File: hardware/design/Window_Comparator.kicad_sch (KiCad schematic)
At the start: 5 parts, among them U1101 LM393

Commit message: Editorial change
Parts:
- R1103: renamed from R1102; value 50k -> 51k
- renumbered R1103 to R1102

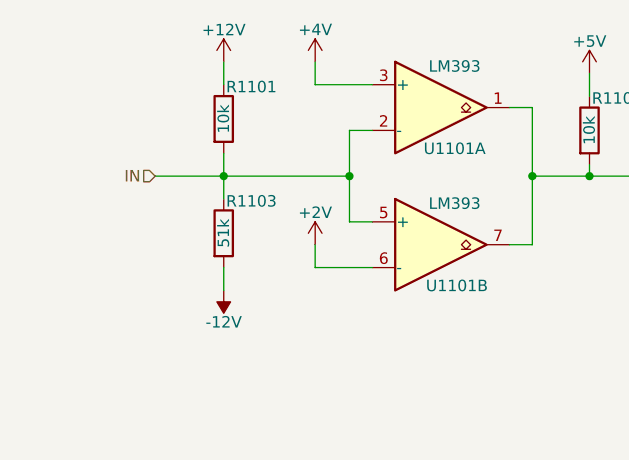
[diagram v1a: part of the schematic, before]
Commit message: Quality assessment - Changes
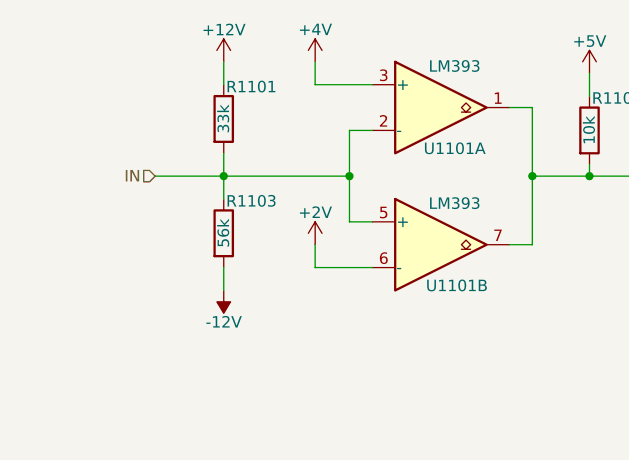
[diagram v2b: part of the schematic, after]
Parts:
- R1101: value 10k -> 33k
- R1103: value 51k -> 56k
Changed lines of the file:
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@@
 			)
 		)
-		(property "Value" "10k"
+		(property "Value" "33k"
 			(at 52.07 46.99 90)
 			(effects
@@
 			)
 		)
-		(property "Value" "51k"
+		(property "Value" "56k"
 			(at 52.07 59.69 90)
 			(effects

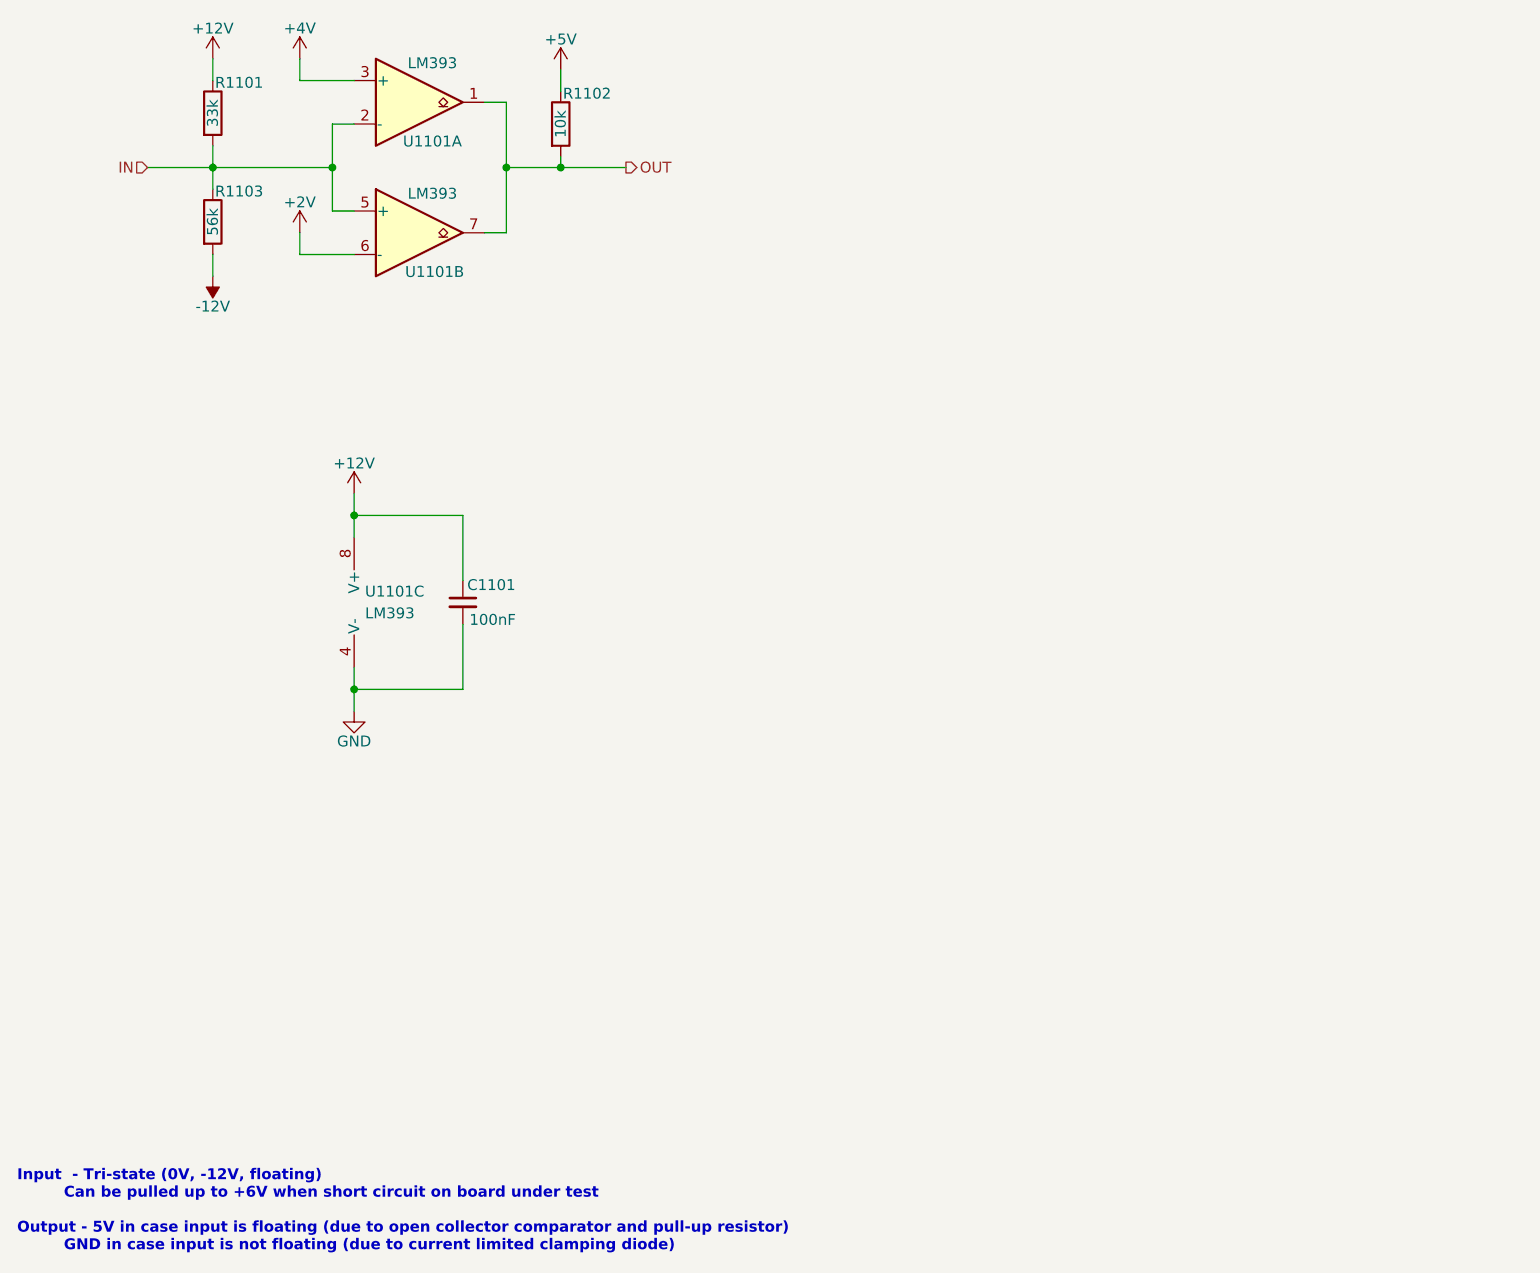
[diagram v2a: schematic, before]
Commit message: Simulating alternative power supply
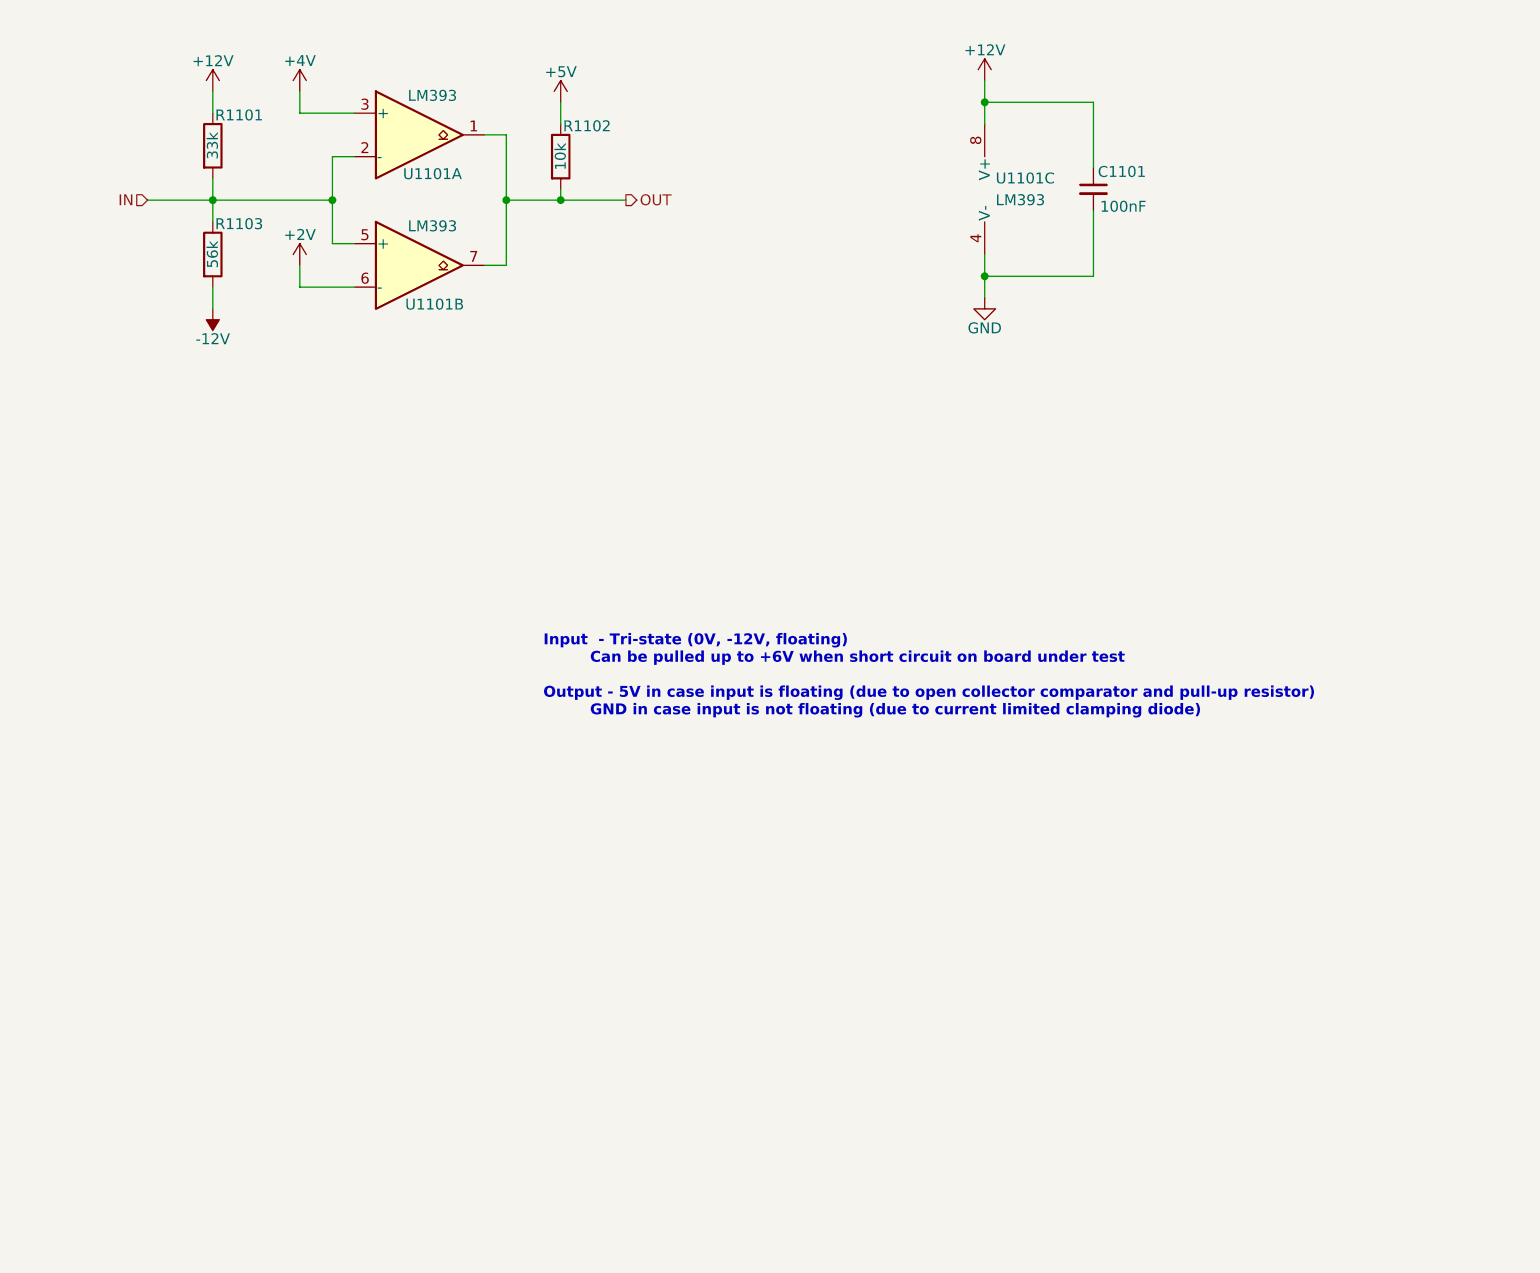
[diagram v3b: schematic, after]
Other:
- moved on the sheet: C1101, R1101, R1102, R1103, U1101A, U1101B, U1101C

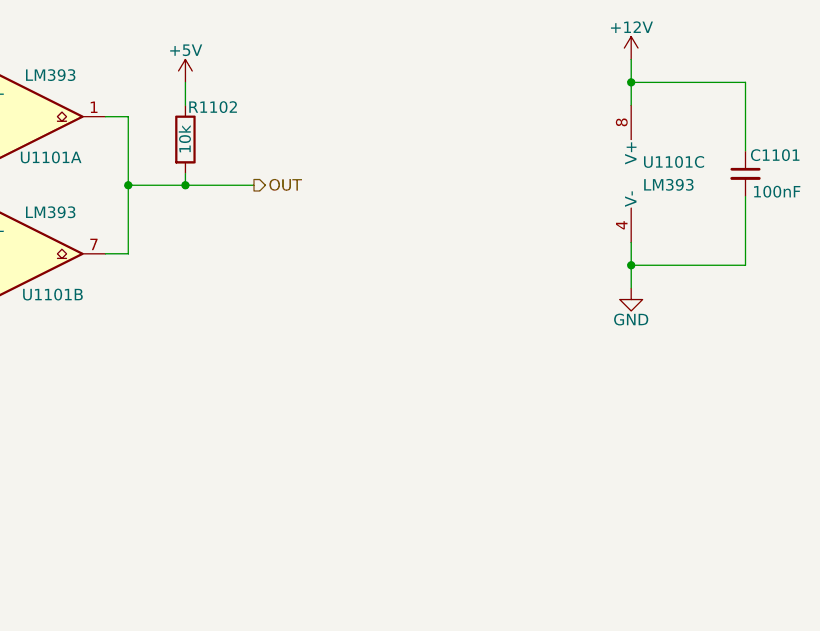
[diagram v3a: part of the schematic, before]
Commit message: Added proof of concept Window comparator
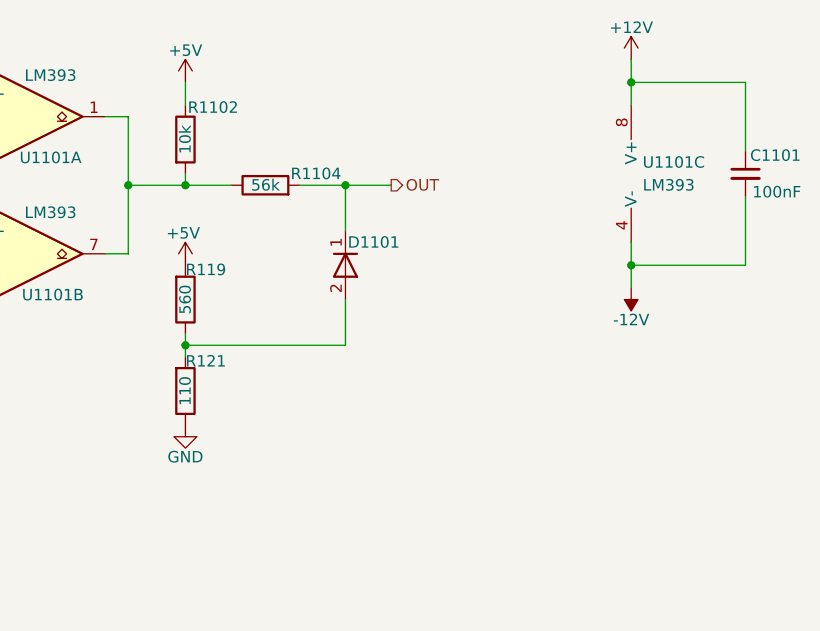
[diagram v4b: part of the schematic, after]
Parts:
- added D1101: D, Diode_THT:D_5W_P10.16mm_Horizontal, symbol Simulation_SPICE:D
- added R1104: 56k, Resistor_THT:R_Axial_DIN0207_L6.3mm_D2.5mm_P7.62mm_Horizontal, symbol Device:R
- added R119: 560, Resistor_THT:R_Axial_DIN0207_L6.3mm_D2.5mm_P7.62mm_Horizontal, symbol Device:R
- added R121: 110, Resistor_THT:R_Axial_DIN0207_L6.3mm_D2.5mm_P7.62mm_Horizontal, symbol Device:R
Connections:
- net +5V: now also R119.2
- net -12V: now also C1101.2, U1101.4 (V-)
- net GND: now also R121.1; no longer C1101.2, U1101.4 (V-)
- net OUT: now also D1101.1 (K), R1104.2; no longer R1102.2, U1101.1, U1101.7
- new net: R1102.2, R1104.1, U1101.1, U1101.7
- new net: D1101.2 (A), R119.1, R121.2

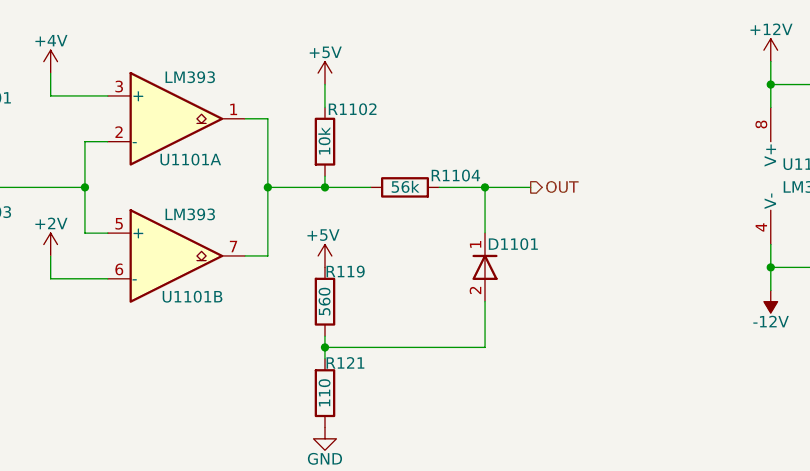
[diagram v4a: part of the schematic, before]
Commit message: Finished proof of concept Window_Comparator and integration test Window_Comparator with Cascaded_74xx165
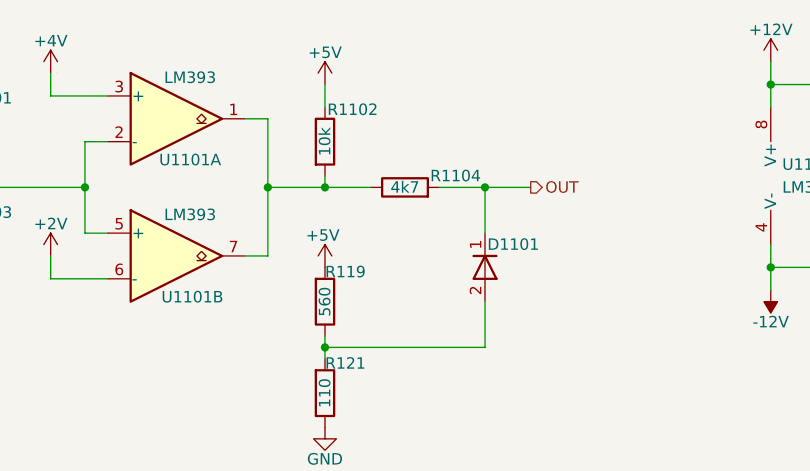
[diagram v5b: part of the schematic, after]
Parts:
- R1104: value 56k -> 4k7
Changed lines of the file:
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@@
 			)
 		)
-		(property "Value" "56k"
+		(property "Value" "4k7"
 			(at 101.6 57.15 90)
 			(effects

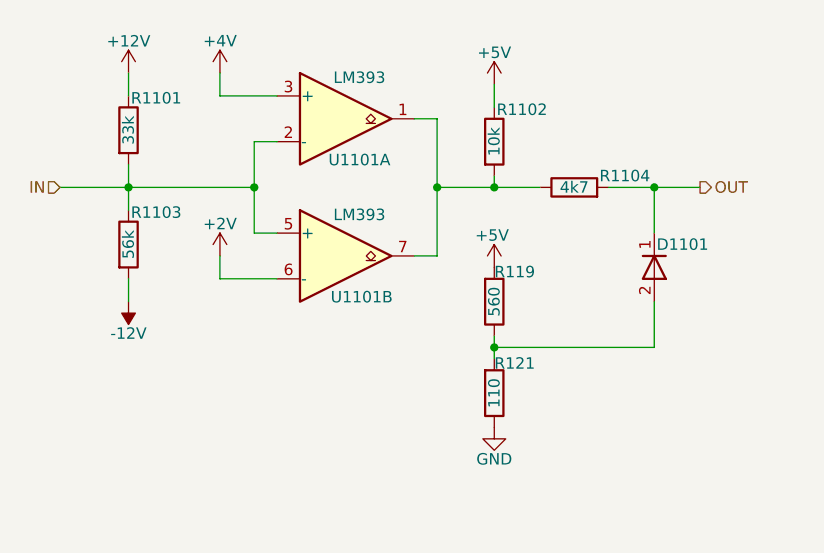
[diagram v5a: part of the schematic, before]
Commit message: Finished proof of concept Relay_Driver
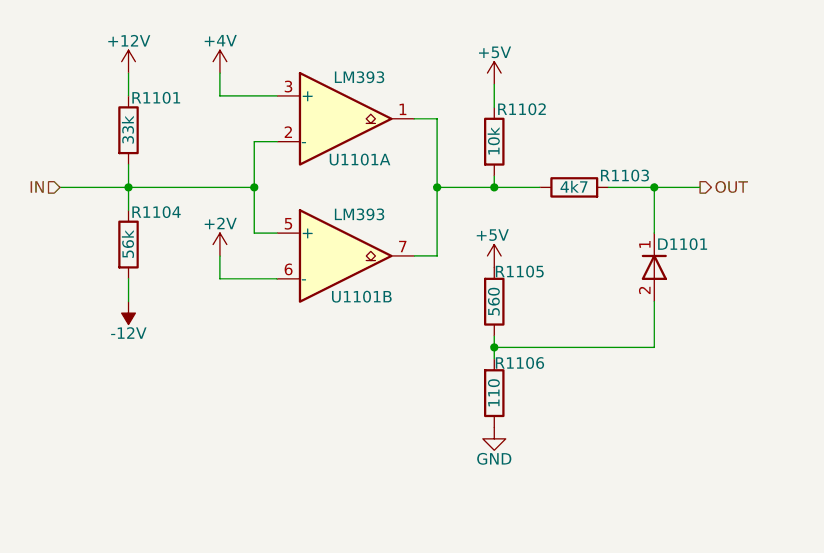
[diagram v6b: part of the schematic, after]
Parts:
- removed R119: 560, Resistor_THT:R_Axial_DIN0207_L6.3mm_D2.5mm_P7.62mm_Horizontal, symbol Device:R
- removed R121: 110, Resistor_THT:R_Axial_DIN0207_L6.3mm_D2.5mm_P7.62mm_Horizontal, symbol Device:R
- added R1105: 560, Resistor_THT:R_Axial_DIN0207_L6.3mm_D2.5mm_P7.62mm_Horizontal, symbol Device:R
- added R1106: 110, Resistor_THT:R_Axial_DIN0207_L6.3mm_D2.5mm_P7.62mm_Horizontal, symbol Device:R
- renumbered R1104 to R1103, R1103 to R1104
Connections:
- net +5V: now also R1105.2
- net GND: now also R1106.1
- net at D1101.2 (A): now also R1105.1, R1106.2

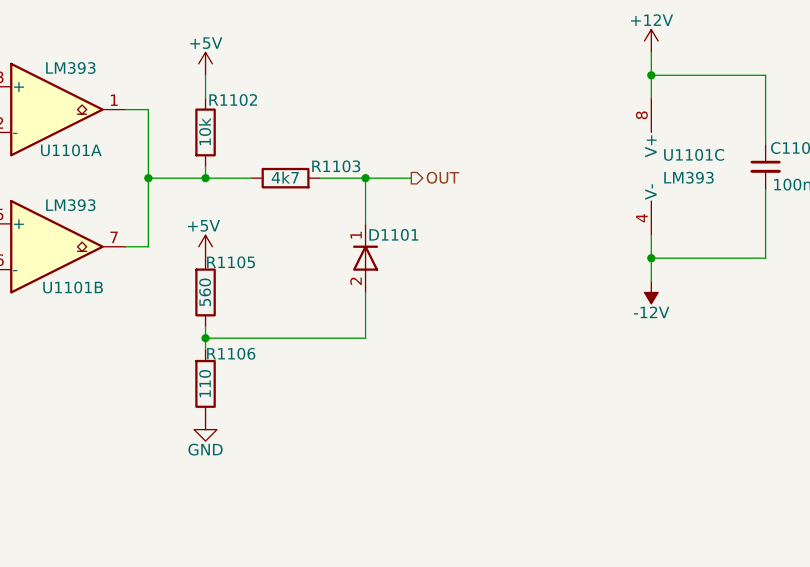
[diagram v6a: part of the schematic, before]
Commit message: Added Setter_Getter proof of concept and Setter_Getter 74xx165 and 74xx595 integration proof of concept
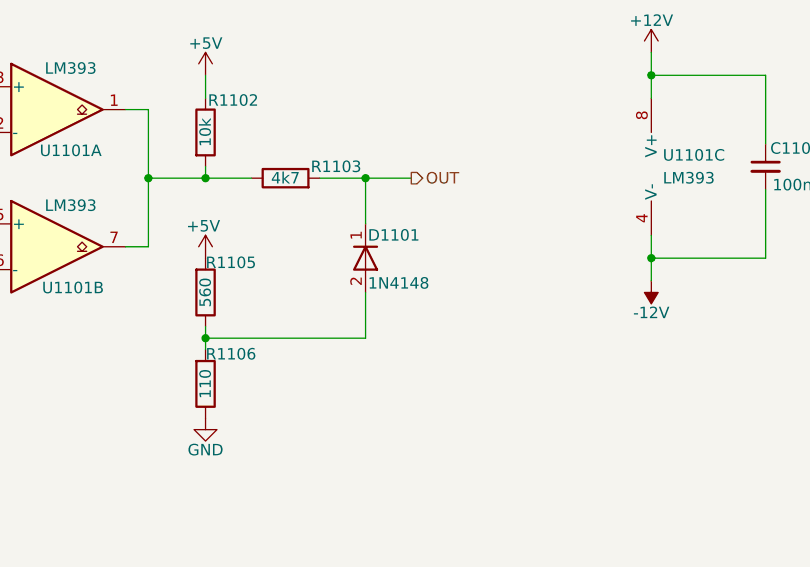
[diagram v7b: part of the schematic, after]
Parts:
- D1101: value D -> 1N4148
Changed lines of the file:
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@@
 			)
 		)
-		(property "Value" "D"
-			(at 113.03 67.3099 90)
+		(property "Value" "1N4148"
+			(at 110.744 68.834 90)
 			(effects
 				(font
@@
 				)
 				(justify left)
-				(hide yes)
 			)
 		)

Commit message: File cleanup
Added final schematics
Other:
- note added: "Input - Tri-state (0V, -12V, floating) Can be pulled up to +6V when there is short circuit on the board under test Output - 5V in case input is floating (due to open collector comparator and pull-up resistor) GND in case input is not floating (due to current limited clamping diode)"
- note removed: "Input - Tri-state (0V, -12V, floating) Can be pulled up to +6V when short circuit on board under test Output - 5V in case input is floating (due to open collector comparator and pull-up resistor) GND in case input is not floating (due to current limited clamping diode)"
- moved on the sheet: R1102
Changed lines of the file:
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@@
 	(title_block
 		(title "VersaLogic board tester")
-		(date "2025-08-13")
-		(rev "1.0.alpha")
+		(date "2025-09-09")
+		(rev "1.0")
 		(comment 1 "Copyright (c) 2025 by Filip Pynckels & Robin Pynckels")
 	)
-	(text "Input  - Tri-state (0V, -12V, floating)\n         Can be pulled up to +6V when short circuit on board under test\n\nOutput - 5V in case input is floating (due to open collector comparator and pull-up resistor)\n         GND in case input is not floating (due to current limited clamping diode)"
+	(text "Input  - Tri-state (0V, -12V, floating)\n         Can be pulled up to +6V when there is short circuit on the board under test\n\nOutput - 5V in case input is floating (due to open collector comparator and pull-up resistor)\n         GND in case input is not floating (due to current limited clamping diode)"
 		(exclude_from_sim no)
-		(at 90.678 107.95 0)
+		(at 90.932 108.458 0)
 		(effects
 			(font
@@
 	(wire
 		(pts
-			(xy 92.71 45.72) (xy 92.71 48.26)
+			(xy 92.71 44.45) (xy 92.71 46.99)
 		)
 		(stroke
@@
 	(wire
 		(pts
-			(xy 92.71 55.88) (xy 92.71 57.15)
+			(xy 92.71 54.61) (xy 92.71 57.15)
 		)
 		(stroke
@@
 	(symbol
 		(lib_id "power:+5V")
-		(at 92.71 45.72 0)
+		(at 92.71 44.45 0)
 		(mirror y)
 		(unit 1)
@@
 		(dnp no)
 		(property "Reference" "#PWR01104"
-			(at 92.71 49.53 0)
+			(at 92.71 48.26 0)
 			(effects
 				(font
@@
 		)
 		(property "Value" "+5V"
-			(at 92.71 42.926 0)
+			(at 92.71 41.656 0)
 			(effects
 				(font
@@
 		)
 		(property "Footprint" ""
-			(at 92.71 45.72 0)
+			(at 92.71 44.45 0)
 			(effects
 				(font
@@
 		)
 		(property "Datasheet" ""
-			(at 92.71 45.72 0)
+			(at 92.71 44.45 0)
 			(effects
 				(font
@@
 		)
 		(property "Description" "Power symbol creates a global label with name \"+5V\""
-			(at 92.71 45.72 0)
+			(at 92.71 44.45 0)
 			(effects
 				(font
@@
 	(symbol
 		(lib_id "Device:R")
-		(at 92.71 52.07 0)
+		(at 92.71 50.8 0)
 		(unit 1)
 		(exclude_from_sim no)
@@
 		(dnp no)
 		(property "Reference" "R1102"
-			(at 92.964 48.514 0)
+			(at 92.964 47.244 0)
 			(effects
 				(font
@@
 		)
 		(property "Value" "10k"
-			(at 92.71 52.07 90)
+			(at 92.71 50.8 90)
 			(effects
 				(font
@@
 		)
 		(property "Footprint" "Resistor_THT:R_Axial_DIN0207_L6.3mm_D2.5mm_P7.62mm_Horizontal"
-			(at 90.932 52.07 90)
+			(at 90.932 50.8 90)
 			(effects
 				(font
@@
 		)
 		(property "Datasheet" "~"
-			(at 92.71 52.07 0)
+			(at 92.71 50.8 0)
 			(effects
 				(font
@@
 		)
 		(property "Description" "Resistor"
-			(at 92.71 52.07 0)
-			(effects
-				(font
+			(at 92.71 50.8 0)
+			(effects
+				(font
